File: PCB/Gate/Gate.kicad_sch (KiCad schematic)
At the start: 746 parts, among them J1 Conn_01x03, J2 Conn_01x03

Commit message: Cap value
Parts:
- C1, C10, C100, C101, C102, C103, C104, C105, C106, C107, C108, C109, C11, C110, C111, C112, C113, C114, C115, C116, C117, C118, C119, C12, C120, C121, C122, C123, C124, C125, C126, C127, C128, C129, C13, C130, C131, C132, C133, C134, C135, C136, C137, C138, C139, C14, C140, C141, C142, C143, C144, C145, C146, C147, C148, C149, C15, C150, C151, C152, C153, C154, C155, C156, C157, C158, C159, C16, C160, C161, C162, C163, C164, C165, C166, C167, C168, C169, C17, C170, C171, C172, C173, C174, C175, C176, C177, C178, C179, C18, C180, C181, C182, C183, C184, C185, C186, C187, C188, C189, C19, C190, C191, C192, C193, C194, C195, C196, C197, C198, C199, C2, C20, C200, C201, C202, C203, C204, C205, C206, C207, C208, C209, C21, C210, C211, C212, C213, C214, C215, C216, C217, C218, C219, C22, C220, C221, C222, C223, C224, C225, C226, C227, C228, C229, C23, C230, C231, C232, C233, C234, C235, C236, C237, C238, C239, C24, C240, C241, C242, C243, C244, C245, C246, C247, C248, C249, C25, C250, C251, C252, C253, C254, C255, C256, C257, C258, C259, C26, C260, C261, C262, C263, C264, C265, C266, C267, C268, C269, C27, C270, C271, C272, C273, C274, C275, C276, C277, C278, C279, C28, C280, C281, C282, C283, C284, C285, C286, C287, C288, C289, C29, C290, C291, C292, C293, C294, C295, C296, C297, C298, C299, C3, C30, C300, C301, C302, C303, C304, C305, C306, C307, C308, C309, C31, C310, C311, C312, C313, C314, C315, C316, C317, C318, C319, C32, C320, C321, C322, C323, C324, C325, C326, C327, C328, C329, C33, C330, C331, C332, C333, C334, C335, C336, C337, C338, C339, C34, C340, C341, C342, C343, C344, C345, C346, C347, C348, C349, C35, C350, C351, C352, C353, C354, C355, C356, C357, C358, C359, C36, C360, C361, C362, C363, C364, C365, C366, C367, C368, C369, C37, C370, C371, C372, C38, C39, C4, C40, C41, C42, C43, C44, C45, C46, C47, C48, C49, C5, C50, C51, C52, C53, C54, C55, C56, C57, C58, C59, C6, C60, C61, C62, C63, C64, C65, C66, C67, C68, C69, C7, C70, C71, C72, C73, C74, C75, C76, C77, C78, C79, C8, C80, C81, C82, C83, C84, C85, C86, C87, C88, C89, C9, C90, C91, C92, C93, C94, C95, C96, C97, C98, C99: value 330nF -> 100nF

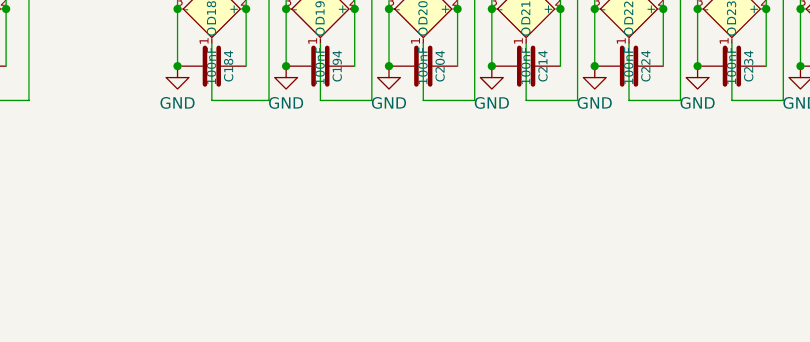
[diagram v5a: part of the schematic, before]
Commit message: tooling holes
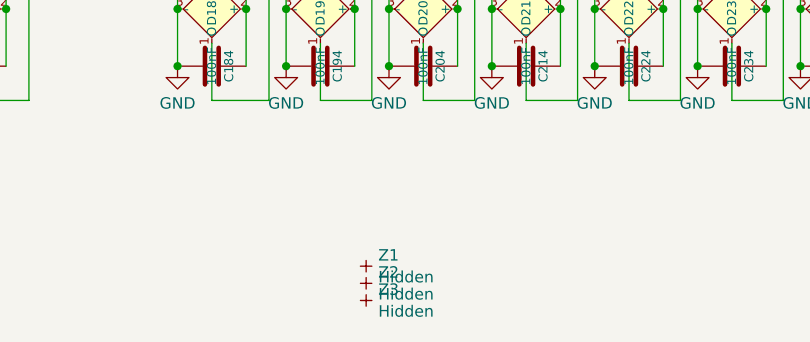
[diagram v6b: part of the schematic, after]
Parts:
- added Z1, Z2, Z3: Hidden, RevK:PCB-Join1, symbol RevK:Hidden
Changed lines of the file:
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@@
     )
   )
+  (symbol (lib_id "RevK:Hidden") (at 252.73 177.8 0) (unit 1)
+    (in_bom no) (on_board yes) (dnp no) (fields_autoplaced)
+    (property "Reference" "Z3" (at 254.0762 176.5879 0)
+      (effects (font (size 1.27 1.27)) (justify left))
+    )
+    (property "Value" "Hidden" (at 254.0762 179.0121 0)
+      (effects (font (size 1.27 1.27)) (justify left))
+    )
+    (property "Footprint" "RevK:PCB-Join1" (at 252.73 175.895 0)
+      (effects (font (size 1.27 1.27)) hide)
+    )
+    (property "Datasheet" "" (at 252.73 177.8 0)
+      (effects (font (size 1.27 1.27)) hide)
+    )
+    (property "Part No" "" (at 252.73 177.8 0)
+      (effects (font (size 1.27 1.27)) hide)
+    )
+    (property "Note" "" (at 252.73 177.8 0)
+      (effects (font (size 1.27 1.27)) hide)
+    )
+    (pin "~")
+    (instances
+      (project "Gate"
+        (path "/46c350bb-7de4-4e81-aafd-4af55e37aab0"
+          (reference "Z3") (unit 1)
+        )
+      )
+    )
+  )
   (symbol (lib_id "RevK:WS2812B-1mm") (at 281.94 145.415 90) (mirror x) (unit 1)
     (in_bom yes) (on_board yes) (dnp no) (fields_autoplaced)
@@
     )
   )
+  (symbol (lib_id "RevK:Hidden") (at 252.73 173.99 0) (unit 1)
+    (in_bom no) (on_board yes) (dnp no) (fields_autoplaced)
+    (property "Reference" "Z1" (at 254.0762 172.7779 0)
+      (effects (font (size 1.27 1.27)) (justify left))
+    )
+    (property "Value" "Hidden" (at 254.0762 175.2021 0)
+      (effects (font (size 1.27 1.27)) (justify left))
+    )
+    (property "Footprint" "RevK:PCB-Join1" (at 252.73 172.085 0)
+      (effects (font (size 1.27 1.27)) hide)
+    )
+    (property "Datasheet" "" (at 252.73 173.99 0)
+      (effects (font (size 1.27 1.27)) hide)
+    )
+    (property "Part No" "" (at 252.73 173.99 0)
+      (effects (font (size 1.27 1.27)) hide)
+    )
+    (property "Note" "" (at 252.73 173.99 0)
+      (effects (font (size 1.27 1.27)) hide)
+    )
+    (pin "~")
+    (instances
+      (project "Gate"
+        (path "/46c350bb-7de4-4e81-aafd-4af55e37aab0"
+          (reference "Z1") (unit 1)
+        )
+      )
+    )
+  )
   (symbol (lib_id "RevK:WS2812B-1mm") (at 121.92 81.915 90) (mirror x) (unit 1)
     (in_bom yes) (on_board yes) (dnp no) (fields_autoplaced)
@@
         )
       )
+    )
+  )
+  (symbol (lib_id "RevK:Hidden") (at 252.73 175.895 0) (unit 1)
+    (in_bom no) (on_board yes) (dnp no) (fields_autoplaced)
+    (property "Reference" "Z2" (at 254.0762 174.6829 0)
+      (effects (font (size 1.27 1.27)) (justify left))
+    )
+    (property "Value" "Hidden" (at 254.0762 177.1071 0)
+      (effects (font (size 1.27 1.27)) (justify left))
+    )
+    (property "Footprint" "RevK:PCB-Join1" (at 252.73 173.99 0)
+      (effects (font (size 1.27 1.27)) hide)
+    )
+    (property "Datasheet" "" (at 252.73 175.895 0)
+      (effects (font (size 1.27 1.27)) hide)
+    )
+    (property "Part No" "" (at 252.73 175.895 0)
+      (effects (font (size 1.27 1.27)) hide)
+    )
+    (property "Note" "" (at 252.73 175.895 0)
+      (effects (font (size 1.27 1.27)) hide)
+    )
+    (pin "~")
+    (instances
+      (project "Gate"
+        (path "/46c350bb-7de4-4e81-aafd-4af55e37aab0"
+          (reference "Z2") (unit 1)
+        )
+      )

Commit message: 498 ring
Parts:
- removed C292, C293, C294, C295, C296, C297, C298, C299, C300, C301, C302, C303, C304, C305, C306, C307, C308, C309: 100nF, RevK:C_0402, symbol Device:C
- removed D292, D293, D294, D295, D296, D297, D298, D299, D300, D301, D302, D303, D304, D305, D306, D307, D308, D309: XL-1010RGBC-WS2812B, RevK:SMD1010, symbol RevK:WS2812B-1mm
- added C1, C10, C100, C101, C102, C103, C104, C105, C106, C107, C108, C109, C11, C110, C111, C112, C113, C114, C115, C116, C117, C12, C13, C14, C15, C16, C17, C18, C19, C2, C20, C21, C22, C23, C24, C25, C26, C27, C28, C29, C3, C30, C31, C32, C33, C34, C35, C36, C37, C38, C39, C4, C40, C409, C41, C410, C411, C412, C413, C414, C415, C416, C417, C418, C419, C42, C420, C421, C422, C423, C424, C425, C426, C427, C428, C429, C43, C430, C431, C432, C433, C434, C435, C44, C45, C46, C47, C48, C49, C5, C50, C51, C52, C53, C54, C55, C56, C57, C58, C59, C6, C60, C61, C62, C63, C64, C65, C66, C67, C68, C69, C7, C70, C71, C72, C73, C74, C75, C76, C77, C78, C79, C8, C80, C81, C82, C83, C84, C85, C86, C87, C88, C89, C9, C90, C91, C92, C93, C94, C95, C96, C97, C98, C99: 100nF, RevK:C_0402, symbol Device:C
- added D1, D10, D100, D101, D102, D103, D104, D105, D106, D107, D108, D109, D11, D110, D111, D112, D113, D114, D115, D116, D117, D12, D13, D14, D15, D16, D17, D18, D19, D2, D20, D21, D22, D23, D24, D25, D26, D27, D28, D29, D3, D30, D31, D32, D33, D34, D35, D36, D37, D38, D39, D4, D40, D409, D41, D410, D411, D412, D413, D414, D415, D416, D417, D418, D419, D42, D420, D421, D422, D423, D424, D425, D426, D427, D428, D429, D43, D430, D431, D432, D433, D434, D435, D44, D45, D46, D47, D48, D49, D5, D50, D51, D52, D53, D54, D55, D56, D57, D58, D59, D6, D60, D61, D62, D63, D64, D65, D66, D67, D68, D69, D7, D70, D71, D72, D73, D74, D75, D76, D77, D78, D79, D8, D80, D81, D82, D83, D84, D85, D86, D87, D88, D89, D9, D90, D91, D92, D93, D94, D95, D96, D97, D98, D99: XL-1010RGBC-WS2812B, RevK:SMD1010, symbol RevK:WS2812B-1mm
- added FID1, FID2, FID3: Fiducial, Fiducial:Fiducial_1mm_Mask2mm, symbol Mechanical:Fiducial
- renumbered C1 to C118, C2 to C119, C3 to C120, C4 to C121, C5 to C122, C6 to C123, C7 to C124, C8 to C125, C9 to C126, C10 to C127, C11 to C128, C12 to C129, C13 to C130, C14 to C131, C15 to C132, C16 to C133, C17 to C134, C18 to C135, C19 to C136, C20 to C137, C21 to C138, C22 to C139, C23 to C140, C24 to C141, C25 to C142, C26 to C143, C27 to C144, C28 to C145, C29 to C146, C30 to C147, C31 to C148, C32 to C149, C33 to C150, C34 to C151, C35 to C152, C36 to C153, C37 to C154, C38 to C155, C39 to C156, C40 to C157, C41 to C158, C42 to C159, C43 to C160, C44 to C161, C45 to C162, C46 to C163, C47 to C164, C48 to C165, C49 to C166, C50 to C167, C51 to C168, C52 to C169, C53 to C170, C54 to C171, C55 to C172, C56 to C173, C57 to C174, C58 to C175, C59 to C176, C60 to C177, C61 to C178, C62 to C179, C63 to C180, C64 to C181, C65 to C182, C66 to C183, C67 to C184, C68 to C185, C69 to C186, C70 to C187, C71 to C188, C72 to C189, C73 to C190, C74 to C191, C75 to C192, C76 to C193, C77 to C194, C78 to C195, C79 to C196, C80 to C197, C81 to C198, C82 to C199, C83 to C200, C84 to C201, C85 to C202, C86 to C203, C87 to C204, C88 to C205, C89 to C206, C90 to C207, C91 to C208, C92 to C209, C93 to C210, C94 to C211, C95 to C212, C96 to C213, C97 to C214, C98 to C215, C99 to C216, C100 to C217, C101 to C218, C102 to C219, C103 to C220, C104 to C221, C105 to C222, C106 to C223, C107 to C224, C108 to C225, C109 to C226, C110 to C227, C111 to C228, C112 to C229, C113 to C230, C114 to C231, C115 to C232, C116 to C233, C117 to C234, C118 to C235, C119 to C236, C120 to C237, C121 to C238, C122 to C239, C123 to C240, C124 to C241, C125 to C242, C126 to C243, C127 to C244, C128 to C245, C129 to C246, C130 to C247, C131 to C248, C132 to C249, C133 to C250, C134 to C251, C135 to C252, C136 to C253, C137 to C254, C138 to C255, C139 to C256, C140 to C257, C141 to C258, C142 to C259, C143 to C260, C144 to C261, C145 to C262, C146 to C263, C147 to C264, C148 to C265, C149 to C266, C150 to C267, C151 to C268, C152 to C269, C153 to C270, C154 to C271, C155 to C272, C156 to C273, C157 to C274, C158 to C275, C159 to C276, C160 to C277, C161 to C278, C162 to C279, C163 to C280, C164 to C281, C165 to C282, C166 to C283, C167 to C284, C168 to C285, C169 to C286, C170 to C287, C171 to C288, C172 to C289, C173 to C290, C174 to C291, C175 to C292, C176 to C293, C177 to C294, C178 to C295, C179 to C296, C180 to C297, C181 to C298, C182 to C299, C183 to C300, C184 to C301, C185 to C302, C186 to C303, C187 to C304, C188 to C305, C189 to C306, C190 to C307, C191 to C308, C192 to C309, C193 to C310, C194 to C311, C195 to C312, C196 to C313, C197 to C314, C198 to C315, C199 to C316, C200 to C317, C201 to C318, C202 to C319, C203 to C320, C204 to C321, C205 to C322, C206 to C323, C207 to C324, C208 to C325, C209 to C326, C210 to C327, C211 to C328, C212 to C329, C213 to C330, C214 to C331, C215 to C332, C216 to C333, C217 to C334, C218 to C335, C219 to C336, C220 to C337, C221 to C338, C222 to C339, C223 to C340, C224 to C341, C225 to C342, C226 to C343, C227 to C344, C228 to C345, C229 to C346, C230 to C347, C231 to C348, C232 to C349, C233 to C350, C234 to C351, C235 to C352, C236 to C353, C237 to C354, C238 to C355, C239 to C356, C240 to C357, C241 to C358, C242 to C359, C243 to C360, C244 to C361, C245 to C362, C246 to C363, C247 to C364, C248 to C365, C249 to C366, C250 to C367, C251 to C368, C252 to C369, C253 to C370, C254 to C371, C255 to C372, C256 to C373, C257 to C374, C258 to C375, C259 to C376, C260 to C377, C261 to C378, C262 to C379, C263 to C380, C264 to C381, C265 to C382, C266 to C383, C267 to C384, C268 to C385, C269 to C386, C270 to C387, C271 to C388, C272 to C389, C273 to C390, C274 to C391, C275 to C392, C276 to C393, C277 to C394, C278 to C395, C279 to C396, C280 to C397, C281 to C398, C282 to C399, C283 to C400, C284 to C401, C285 to C402, C286 to C403, C287 to C404, C288 to C405, C289 to C406, C290 to C407, C291 to C408, C310 to C436, C311 to C437, C312 to C438, C313 to C439, C314 to C440, C315 to C441, C316 to C442, C317 to C443, C318 to C444, C319 to C445, C320 to C446, C321 to C447, C322 to C448, C323 to C449, C324 to C450, C325 to C451, C326 to C452, C327 to C453, C328 to C454, C329 to C455, C330 to C456, C331 to C457, C332 to C458, C333 to C459, C334 to C460, C335 to C461, C336 to C462, C337 to C463, C338 to C464, C339 to C465, C340 to C466, C341 to C467, C342 to C468, C343 to C469, C344 to C470, C345 to C471, C346 to C472, C347 to C473, C348 to C474, C349 to C475, C350 to C476, C351 to C477, C352 to C478, C353 to C479, C354 to C480, C355 to C481, C356 to C482, C357 to C483, C358 to C484, C359 to C485, C360 to C486, C361 to C487, C362 to C488, C363 to C489, C364 to C490, C365 to C491, C366 to C492, C367 to C493, C368 to C494, C369 to C495, C370 to C496, C371 to C497, C372 to C498, D1 to D118, D2 to D119, D3 to D120, D4 to D121, D5 to D122, D6 to D123, D7 to D124, D8 to D125, D9 to D126, D10 to D127, D11 to D128, D12 to D129, D13 to D130, D14 to D131, D15 to D132, D16 to D133, D17 to D134, D18 to D135, D19 to D136, D20 to D137, D21 to D138, D22 to D139, D23 to D140, D24 to D141, D25 to D142, D26 to D143, D27 to D144, D28 to D145, D29 to D146, D30 to D147, D31 to D148, D32 to D149, D33 to D150, D34 to D151, D35 to D152, D36 to D153, D37 to D154, D38 to D155, D39 to D156, D40 to D157, D41 to D158, D42 to D159, D43 to D160, D44 to D161, D45 to D162, D46 to D163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
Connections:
- net GND: now also C1.2, C10.2, C100.2, C101.2, C102.2, C103.2, C104.2, C105.2, C106.2, C107.2, C108.2, C109.2, C11.2, C110.2, C111.2, C112.2, C113.2, C114.2, C115.2, C116.2, C117.2, C12.2, C13.2, C14.2, C15.2, C16.2, C17.2, C18.2, C19.2, C2.2, C20.2, C21.2, C22.2, C23.2, C24.2, C25.2, C26.2, C27.2, C28.2, C29.2, C3.2, C30.2, C31.2, C32.2, C33.2, C34.2, C35.2, C36.2, C37.2, C38.2, C39.2, C4.2, C40.2, C409.2, C41.2, C410.2, C411.2, C412.2, C413.2, C414.2, C415.2, C416.2, C417.2, C418.2, C419.2, C42.2, C420.2, C421.2, C422.2, C423.2, C424.2, C425.2, C426.2, C427.2, C428.2, C429.2, C43.2, C430.2, C431.2, C432.2, C433.2, C434.2, C435.2, C44.2, C45.2, C46.2, C47.2, C48.2, C49.2, C5.2, C50.2, C51.2, C52.2, C53.2, C54.2, C55.2, C56.2, C57.2, C58.2, C59.2, C6.2, C60.2, C61.2, C62.2, C63.2, C64.2, C65.2, C66.2, C67.2, C68.2, C69.2, C7.2, C70.2, C71.2, C72.2, C73.2, C74.2, C75.2, C76.2, C77.2, C78.2, C79.2, C8.2, C80.2, C81.2, C82.2, C83.2, C84.2, C85.2, C86.2, C87.2, C88.2, C89.2, C9.2, C90.2, C91.2, C92.2, C93.2, C94.2, C95.2, C96.2, C97.2, C98.2, C99.2, D1.3 (-), D10.3 (-), D100.3 (-), D101.3 (-), D102.3 (-), D103.3 (-), D104.3 (-), D105.3 (-), D106.3 (-), D107.3 (-), D108.3 (-), D109.3 (-), D11.3 (-), D110.3 (-), D111.3 (-), D112.3 (-), D113.3 (-), D114.3 (-), D115.3 (-), D116.3 (-), D117.3 (-), D12.3 (-), D13.3 (-), D14.3 (-), D15.3 (-), D16.3 (-), D17.3 (-), D18.3 (-), D19.3 (-), D2.3 (-), D20.3 (-), D21.3 (-), D22.3 (-), D23.3 (-), D24.3 (-), D25.3 (-), D26.3 (-), D27.3 (-), D28.3 (-), D29.3 (-), D3.3 (-), D30.3 (-), D31.3 (-), D32.3 (-), D33.3 (-), D34.3 (-), D35.3 (-), D36.3 (-), D37.3 (-), D38.3 (-), D39.3 (-), D4.3 (-), D40.3 (-), D409.3 (-), D41.3 (-), D410.3 (-), D411.3 (-), D412.3 (-), D413.3 (-), D414.3 (-), D415.3 (-), D416.3 (-), D417.3 (-), D418.3 (-), D419.3 (-), D42.3 (-), D420.3 (-), D421.3 (-), D422.3 (-), D423.3 (-), D424.3 (-), D425.3 (-), D426.3 (-), D427.3 (-), D428.3 (-), D429.3 (-), D43.3 (-), D430.3 (-), D431.3 (-), D432.3 (-), D433.3 (-), D434.3 (-), D435.3 (-), D44.3 (-), D45.3 (-), D46.3 (-), D47.3 (-), D48.3 (-), D49.3 (-), D5.3 (-), D50.3 (-), D51.3 (-), D52.3 (-), D53.3 (-), D54.3 (-), D55.3 (-), D56.3 (-), D57.3 (-), D58.3 (-), D59.3 (-), D6.3 (-), D60.3 (-), D61.3 (-), D62.3 (-), D63.3 (-), D64.3 (-), D65.3 (-), D66.3 (-), D67.3 (-), D68.3 (-), D69.3 (-), D7.3 (-), D70.3 (-), D71.3 (-), D72.3 (-), D73.3 (-), D74.3 (-), D75.3 (-), D76.3 (-), D77.3 (-), D78.3 (-), D79.3 (-), D8.3 (-), D80.3 (-), D81.3 (-), D82.3 (-), D83.3 (-), D84.3 (-), D85.3 (-), D86.3 (-), D87.3 (-), D88.3 (-), D89.3 (-), D9.3 (-), D90.3 (-), D91.3 (-), D92.3 (-), D93.3 (-), D94.3 (-), D95.3 (-), D96.3 (-), D97.3 (-), D98.3 (-), D99.3 (-)
- net VCC: now also C1.1, C10.1, C100.1, C101.1, C102.1, C103.1, C104.1, C105.1, C106.1, C107.1, C108.1, C109.1, C11.1, C110.1, C111.1, C112.1, C113.1, C114.1, C115.1, C116.1, C117.1, C12.1, C13.1, C14.1, C15.1, C16.1, C17.1, C18.1, C19.1, C2.1, C20.1, C21.1, C22.1, C23.1, C24.1, C25.1, C26.1, C27.1, C28.1, C29.1, C3.1, C30.1, C31.1, C32.1, C33.1, C34.1, C35.1, C36.1, C37.1, C38.1, C39.1, C4.1, C40.1, C409.1, C41.1, C410.1, C411.1, C412.1, C413.1, C414.1, C415.1, C416.1, C417.1, C418.1, C419.1, C42.1, C420.1, C421.1, C422.1, C423.1, C424.1, C425.1, C426.1, C427.1, C428.1, C429.1, C43.1, C430.1, C431.1, C432.1, C433.1, C434.1, C435.1, C44.1, C45.1, C46.1, C47.1, C48.1, C49.1, C5.1, C50.1, C51.1, C52.1, C53.1, C54.1, C55.1, C56.1, C57.1, C58.1, C59.1, C6.1, C60.1, C61.1, C62.1, C63.1, C64.1, C65.1, C66.1, C67.1, C68.1, C69.1, C7.1, C70.1, C71.1, C72.1, C73.1, C74.1, C75.1, C76.1, C77.1, C78.1, C79.1, C8.1, C80.1, C81.1, C82.1, C83.1, C84.1, C85.1, C86.1, C87.1, C88.1, C89.1, C9.1, C90.1, C91.1, C92.1, C93.1, C94.1, C95.1, C96.1, C97.1, C98.1, C99.1, D1.2 (+), D10.2 (+), D100.2 (+), D101.2 (+), D102.2 (+), D103.2 (+), D104.2 (+), D105.2 (+), D106.2 (+), D107.2 (+), D108.2 (+), D109.2 (+), D11.2 (+), D110.2 (+), D111.2 (+), D112.2 (+), D113.2 (+), D114.2 (+), D115.2 (+), D116.2 (+), D117.2 (+), D12.2 (+), D13.2 (+), D14.2 (+), D15.2 (+), D16.2 (+), D17.2 (+), D18.2 (+), D19.2 (+), D2.2 (+), D20.2 (+), D21.2 (+), D22.2 (+), D23.2 (+), D24.2 (+), D25.2 (+), D26.2 (+), D27.2 (+), D28.2 (+), D29.2 (+), D3.2 (+), D30.2 (+), D31.2 (+), D32.2 (+), D33.2 (+), D34.2 (+), D35.2 (+), D36.2 (+), D37.2 (+), D38.2 (+), D39.2 (+), D4.2 (+), D40.2 (+), D409.2 (+), D41.2 (+), D410.2 (+), D411.2 (+), D412.2 (+), D413.2 (+), D414.2 (+), D415.2 (+), D416.2 (+), D417.2 (+), D418.2 (+), D419.2 (+), D42.2 (+), D420.2 (+), D421.2 (+), D422.2 (+), D423.2 (+), D424.2 (+), D425.2 (+), D426.2 (+), D427.2 (+), D428.2 (+), D429.2 (+), D43.2 (+), D430.2 (+), D431.2 (+), D432.2 (+), D433.2 (+), D434.2 (+), D435.2 (+), D44.2 (+), D45.2 (+), D46.2 (+), D47.2 (+), D48.2 (+), D49.2 (+), D5.2 (+), D50.2 (+), D51.2 (+), D52.2 (+), D53.2 (+), D54.2 (+), D55.2 (+), D56.2 (+), D57.2 (+), D58.2 (+), D59.2 (+), D6.2 (+), D60.2 (+), D61.2 (+), D62.2 (+), D63.2 (+), D64.2 (+), D65.2 (+), D66.2 (+), D67.2 (+), D68.2 (+), D69.2 (+), D7.2 (+), D70.2 (+), D71.2 (+), D72.2 (+), D73.2 (+), D74.2 (+), D75.2 (+), D76.2 (+), D77.2 (+), D78.2 (+), D79.2 (+), D8.2 (+), D80.2 (+), D81.2 (+), D82.2 (+), D83.2 (+), D84.2 (+), D85.2 (+), D86.2 (+), D87.2 (+), D88.2 (+), D89.2 (+), D9.2 (+), D90.2 (+), D91.2 (+), D92.2 (+), D93.2 (+), D94.2 (+), D95.2 (+), D96.2 (+), D97.2 (+), D98.2 (+), D99.2 (+)
- net at D118.4 (I): now also D117.1 (O); no longer J1.2 (Pin_2)
- net at D408.1 (O): now also D409.4 (I)
- net at D436.4 (I): now also D435.1 (O)
- new net: D52.1 (O), D53.4 (I)
- new net: D51.1 (O), D52.4 (I)
- new net: D76.1 (O), D77.4 (I)
- new net: D75.1 (O), D76.4 (I)
- new net: D68.1 (O), D69.4 (I)
- new net: D67.1 (O), D68.4 (I)
- new net: D63.1 (O), D64.4 (I)
- new net: D62.1 (O), D63.4 (I)
- new net: D27.1 (O), D28.4 (I)
- new net: D26.1 (O), D27.4 (I)
- new net: D8.1 (O), D9.4 (I)
- new net: D7.1 (O), D8.4 (I)
- new net: D15.1 (O), D16.4 (I)
- new net: D14.1 (O), D15.4 (I)
- new net: D60.1 (O), D61.4 (I)
- new net: D59.1 (O), D60.4 (I)
- new net: D47.1 (O), D48.4 (I)
- new net: D46.1 (O), D47.4 (I)
- new net: D13.1 (O), D14.4 (I)
- new net: D12.1 (O), D13.4 (I)
- new net: D11.1 (O), D12.4 (I)
- new net: D78.1 (O), D79.4 (I)
- new net: D77.1 (O), D78.4 (I)
- new net: D32.1 (O), D33.4 (I)
- new net: D31.1 (O), D32.4 (I)
- new net: D50.1 (O), D51.4 (I)
- new net: D49.1 (O), D50.4 (I)
- new net: D86.1 (O), D87.4 (I)
- new net: D85.1 (O), D86.4 (I)
- new net: D17.1 (O), D18.4 (I)
- new net: D16.1 (O), D17.4 (I)
- new net: D110.1 (O), D111.4 (I)
- new net: D109.1 (O), D110.4 (I)
- new net: D79.1 (O), D80.4 (I)
- new net: D71.1 (O), D72.4 (I)
- new net: D70.1 (O), D71.4 (I)
- new net: D116.1 (O), D117.4 (I)
- new net: D35.1 (O), D36.4 (I)
- new net: D34.1 (O), D35.4 (I)
- new net: D10.1 (O), D11.4 (I)
- new net: D89.1 (O), D90.4 (I)
- new net: D88.1 (O), D89.4 (I)
- new net: D420.1 (O), D421.4 (I)
- new net: D419.1 (O), D420.4 (I)
- new net: D108.1 (O), D109.4 (I)
- new net: D42.1 (O), D43.4 (I)
- new net: D41.1 (O), D42.4 (I)
- new net: D92.1 (O), D93.4 (I)
- new net: D91.1 (O), D92.4 (I)
- new net: D425.1 (O), D426.4 (I)
- new net: D424.1 (O), D425.4 (I)
- new net: D428.1 (O), D429.4 (I)
- new net: D427.1 (O), D428.4 (I)
- new net: D426.1 (O), D427.4 (I)
- new net: D1.1 (O), D2.4 (I)
- new net: D1.4 (I), J1.2 (Pin_2)
- new net: D115.1 (O), D116.4 (I)
- new net: D114.1 (O), D115.4 (I)
- new net: D44.1 (O), D45.4 (I)
- new net: D43.1 (O), D44.4 (I)
- new net: D84.1 (O), D85.4 (I)
- new net: D83.1 (O), D84.4 (I)
- new net: D93.1 (O), D94.4 (I)
- new net: D105.1 (O), D106.4 (I)
- new net: D104.1 (O), D105.4 (I)
- new net: D39.1 (O), D40.4 (I)
- new net: D38.1 (O), D39.4 (I)
- new net: D18.1 (O), D19.4 (I)
- new net: D433.1 (O), D434.4 (I)
- new net: D432.1 (O), D433.4 (I)
- new net: D80.1 (O), D81.4 (I)
- new net: D107.1 (O), D108.4 (I)
- new net: D22.1 (O), D23.4 (I)
- new net: D21.1 (O), D22.4 (I)
- new net: D422.1 (O), D423.4 (I)
- new net: D421.1 (O), D422.4 (I)
- new net: D111.1 (O), D112.4 (I)
- new net: D53.1 (O), D54.4 (I)
- new net: D30.1 (O), D31.4 (I)
- new net: D95.1 (O), D96.4 (I)
- new net: D94.1 (O), D95.4 (I)
- new net: D37.1 (O), D38.4 (I)
- new net: D36.1 (O), D37.4 (I)
- new net: D411.1 (O), D412.4 (I)
- new net: D410.1 (O), D411.4 (I)
- new net: D434.1 (O), D435.4 (I)
- new net: D409.1 (O), D410.4 (I)
- new net: D2.1 (O), D3.4 (I)
- new net: D96.1 (O), D97.4 (I)
- new net: D414.1 (O), D415.4 (I)
- new net: D413.1 (O), D414.4 (I)
- new net: D6.1 (O), D7.4 (I)
- new net: D430.1 (O), D431.4 (I)
- new net: D429.1 (O), D430.4 (I)
- new net: D90.1 (O), D91.4 (I)
- new net: D431.1 (O), D432.4 (I)
- new net: D33.1 (O), D34.4 (I)
- new net: D24.1 (O), D25.4 (I)
- new net: D23.1 (O), D24.4 (I)
- new net: D4.1 (O), D5.4 (I)
- new net: D3.1 (O), D4.4 (I)
- new net: D57.1 (O), D58.4 (I)
- new net: D56.1 (O), D57.4 (I)
- new net: D69.1 (O), D70.4 (I)
- new net: D412.1 (O), D413.4 (I)
- new net: D112.1 (O), D113.4 (I)
- new net: D98.1 (O), D99.4 (I)
- new net: D97.1 (O), D98.4 (I)
- new net: D20.1 (O), D21.4 (I)
- new net: D19.1 (O), D20.4 (I)
- new net: D29.1 (O), D30.4 (I)
- new net: D100.4 (I), D99.1 (O)
- new net: D61.1 (O), D62.4 (I)
- new net: D101.1 (O), D102.4 (I)
- new net: D100.1 (O), D101.4 (I)
- new net: D58.1 (O), D59.4 (I)
- new net: D28.1 (O), D29.4 (I)
- new net: D10.4 (I), D9.1 (O)
- new net: D64.1 (O), D65.4 (I)
- new net: D81.1 (O), D82.4 (I)
- new net: D103.1 (O), D104.4 (I)
- new net: D48.1 (O), D49.4 (I)
- new net: D416.1 (O), D417.4 (I)
- new net: D415.1 (O), D416.4 (I)
- new net: D45.1 (O), D46.4 (I)
- new net: D54.1 (O), D55.4 (I)
- new net: D102.1 (O), D103.4 (I)
- new net: D82.1 (O), D83.4 (I)
- new net: D25.1 (O), D26.4 (I)
- new net: D5.1 (O), D6.4 (I)
- new net: D65.1 (O), D66.4 (I)
- new net: D55.1 (O), D56.4 (I)
- new net: D113.1 (O), D114.4 (I)
- new net: D423.1 (O), D424.4 (I)
- new net: D74.1 (O), D75.4 (I)
- new net: D40.1 (O), D41.4 (I)
- new net: D418.1 (O), D419.4 (I)
- new net: D417.1 (O), D418.4 (I)
- new net: D72.1 (O), D73.4 (I)
- new net: D106.1 (O), D107.4 (I)
- new net: D66.1 (O), D67.4 (I)
- new net: D73.1 (O), D74.4 (I)
- new net: D87.1 (O), D88.4 (I)
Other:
- moved on the sheet: C436, C437, C438, C439, C440, C441, C442, C443, C444, C445, C446, C447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

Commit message: Can no order JLC
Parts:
- J1, J2: now left out of the parts list
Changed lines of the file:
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@@
   )
   (symbol (lib_id "Connector_Generic:Conn_01x03") (at 484.505 100.33 90) (mirror x) (unit 1)
-    (in_bom yes) (on_board yes) (dnp no)
+    (in_bom no) (on_board yes) (dnp no)
     (property "Reference" "J2" (at 483.2929 102.362 0)
       (effects (font (size 1.27 1.27)) (justify left))
@@
   )
   (symbol (lib_id "Connector_Generic:Conn_01x03") (at -123.19 19.685 90) (unit 1)
-    (in_bom yes) (on_board yes) (dnp no)
+    (in_bom no) (on_board yes) (dnp no)
     (property "Reference" "J1" (at -115.2357 19.685 0)
       (effects (font (size 1.27 1.27)))
